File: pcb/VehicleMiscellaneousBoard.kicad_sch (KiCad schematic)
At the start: 13 parts, among them J2 Conn_02x05_Top_Bottom, J4 B8B-XH-A, U1 OpenMV H7+, U2 Seeed_Studio_XIAO-ESP32-S3-Se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

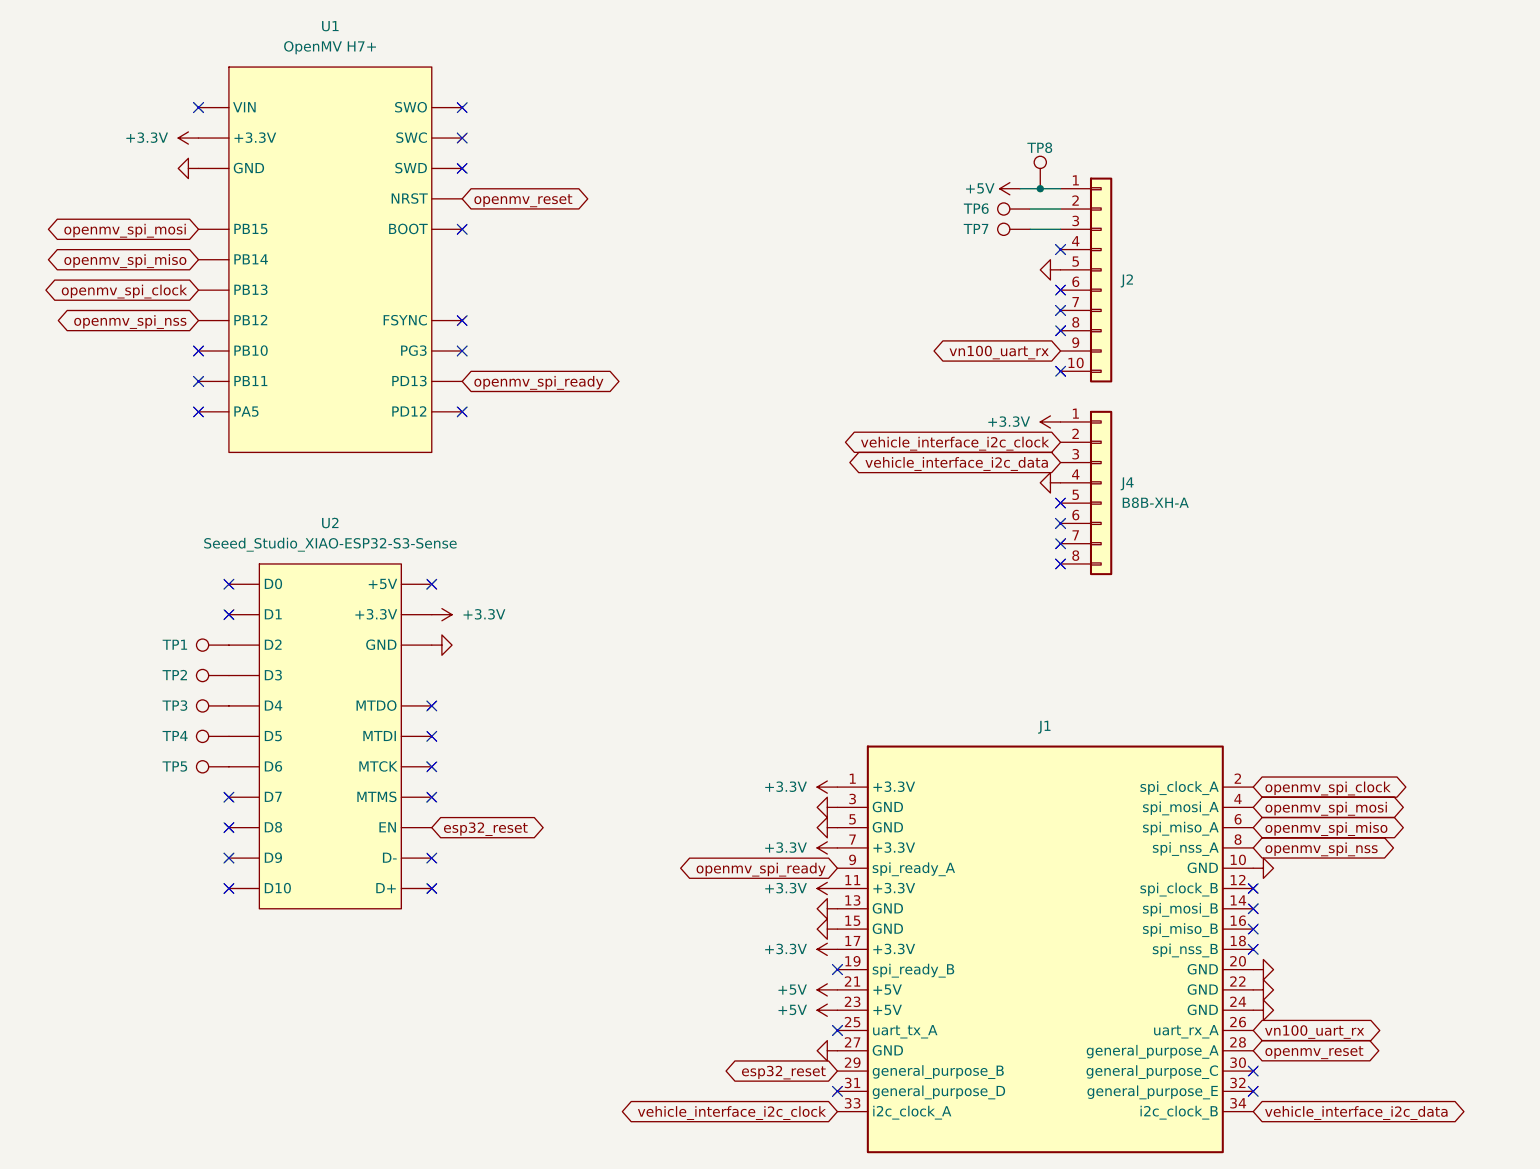
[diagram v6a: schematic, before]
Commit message: Updated MCU pin-outs for `VehicleFlightComputer`.
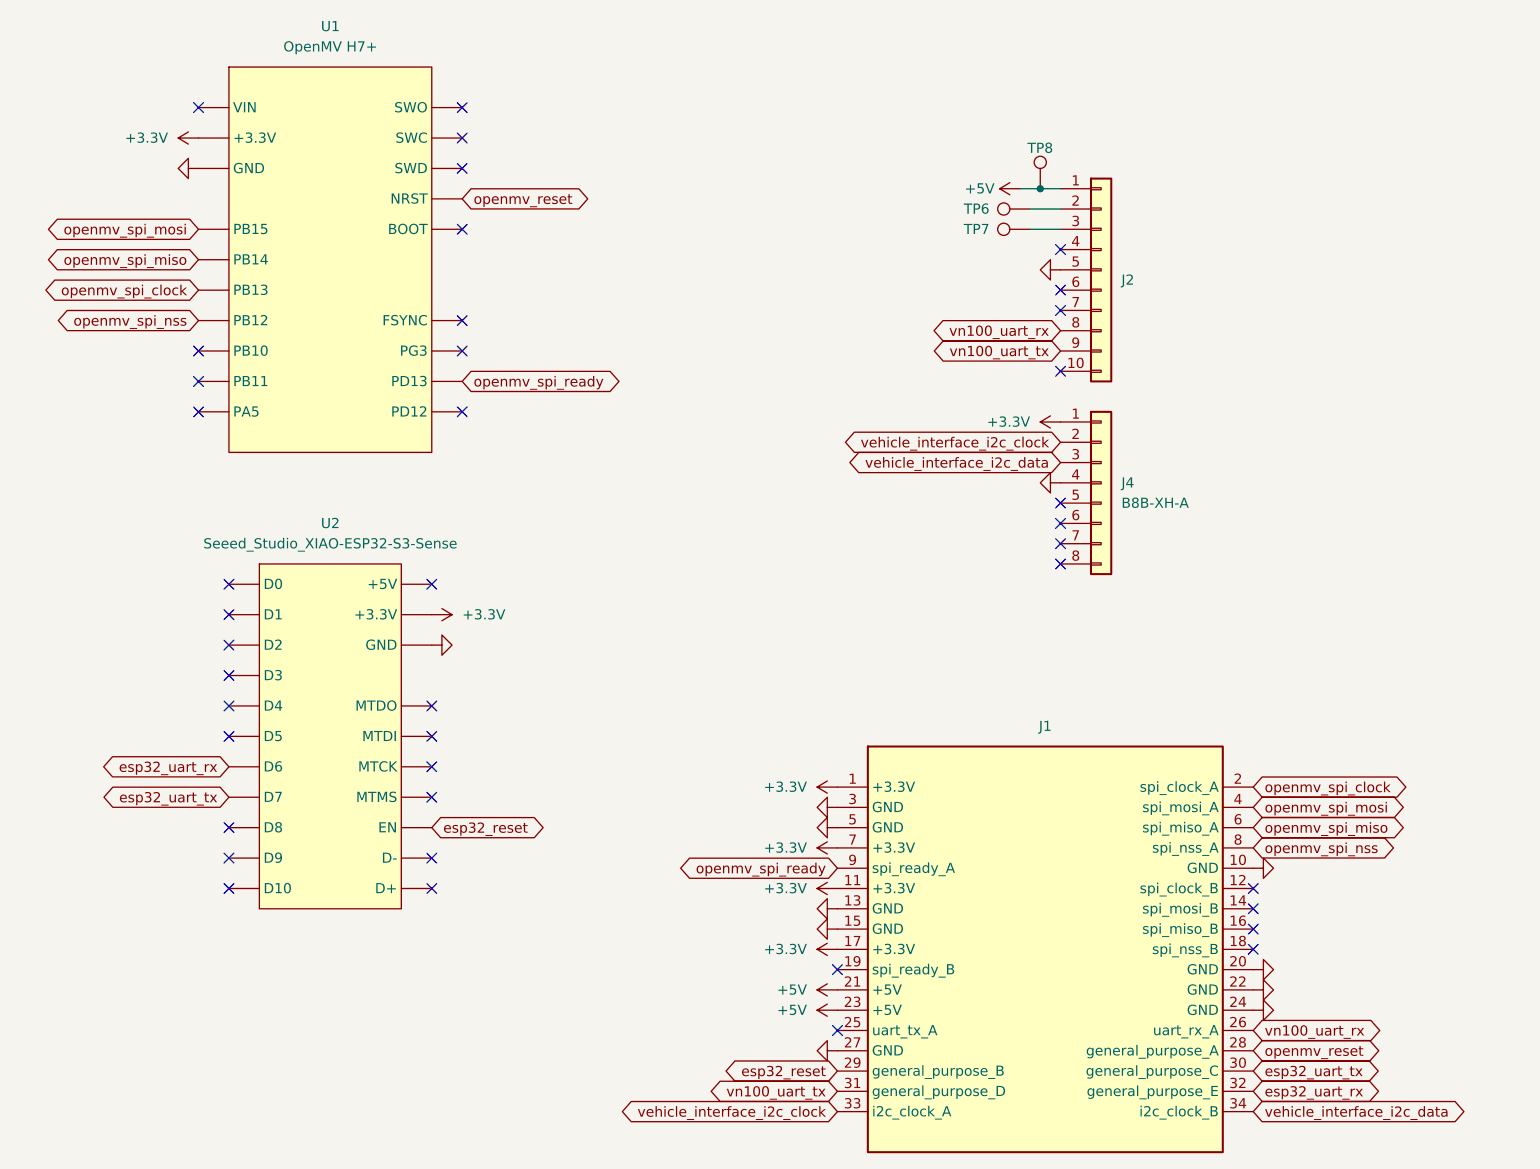
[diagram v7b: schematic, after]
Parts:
- removed TP1, TP2, TP3, TP4, TP5: TestPoint, TestPoint:TestPoint_Pad_1.0x1.0mm, symbol Connector:TestPoint
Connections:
- net vn100_uart_rx: now also J2.8 (Pin_8); no longer J2.9 (Pin_9)
- net esp32_uart_tx: now reaches J1.30 (general_purpose_C)
- net esp32_uart_tx: now also U2.D7
- net vn100_uart_tx: now reaches J1.31 (general_purpose_D)
- net vn100_uart_tx: now also J2.9 (Pin_9)
- net esp32_uart_rx: now reaches J1.32 (general_purpose_E)
- net esp32_uart_rx: now also U2.D6
- no-connect marks 42 -> 41

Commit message: Finalized `VMISC-R2`.
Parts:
- removed TP6, TP7, TP8: TestPoint, TestPoint:TestPoint_Pad_1.0x1.0mm, symbol Connector:TestPoint
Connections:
- net +3.3V: now also J4.5 (Pin_5), J4.7 (Pin_7)
- net +5V: now also J2.3 (Pin_3)
- net GND: now also J2.2 (Pin_2), J2.4 (Pin_4), J4.6 (Pin_6), J4.8 (Pin_8); no longer J2.5 (Pin_5)
- no-connect marks 41 -> 37
